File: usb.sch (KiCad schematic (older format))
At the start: 46 parts, among them J6 USB_B_F_X2, J7 USB_B_F_X2, U10 HLF-W2, U4 GL850G, X1 12MHz

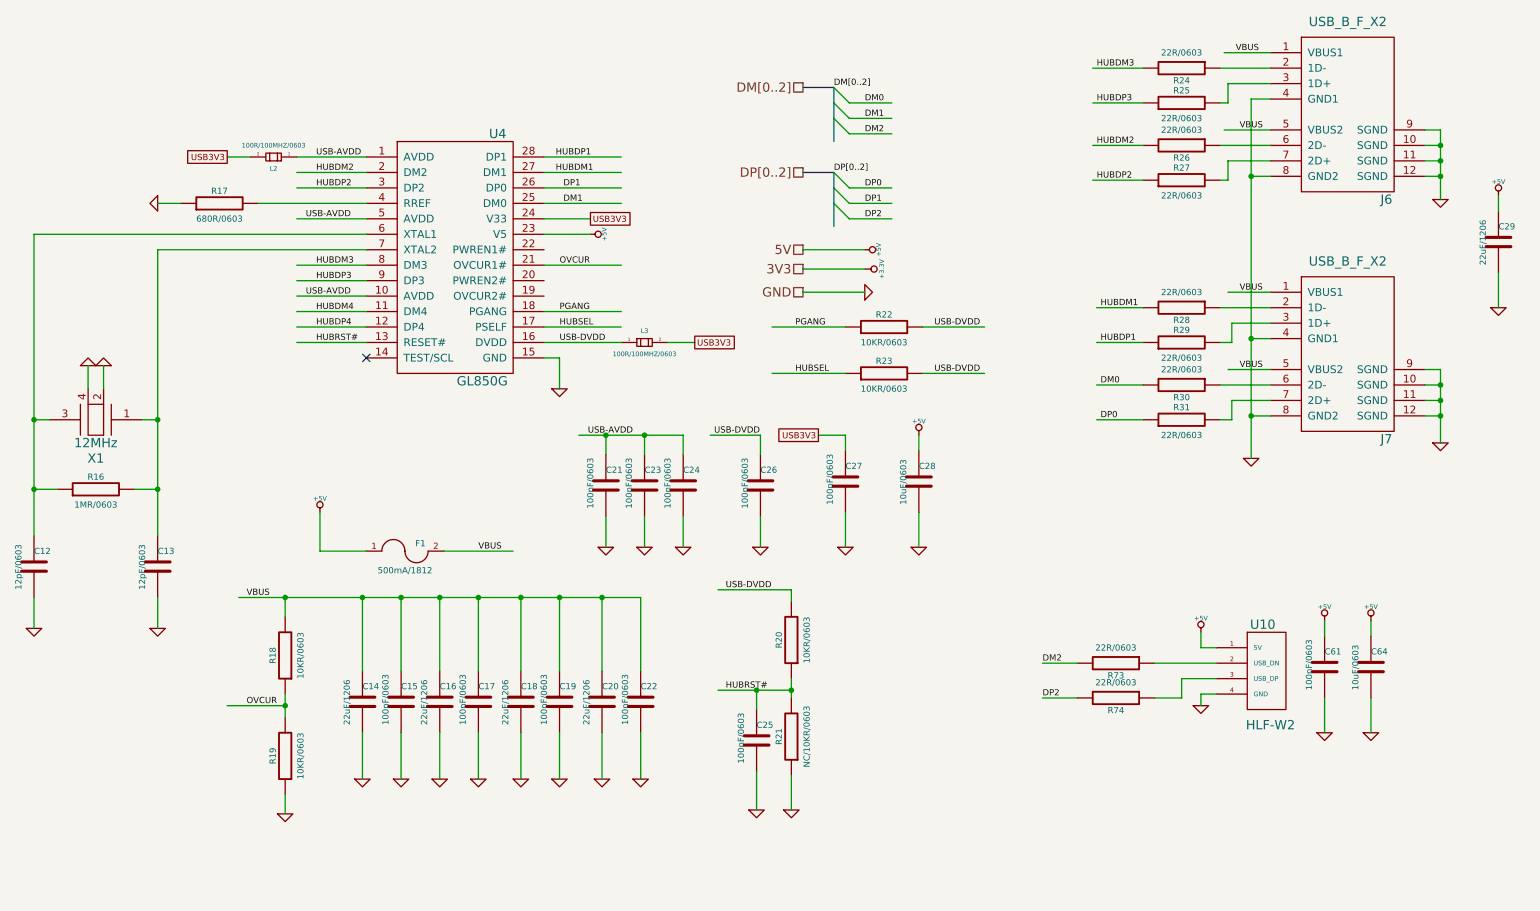
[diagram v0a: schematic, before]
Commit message: 1.4
Fix some issues
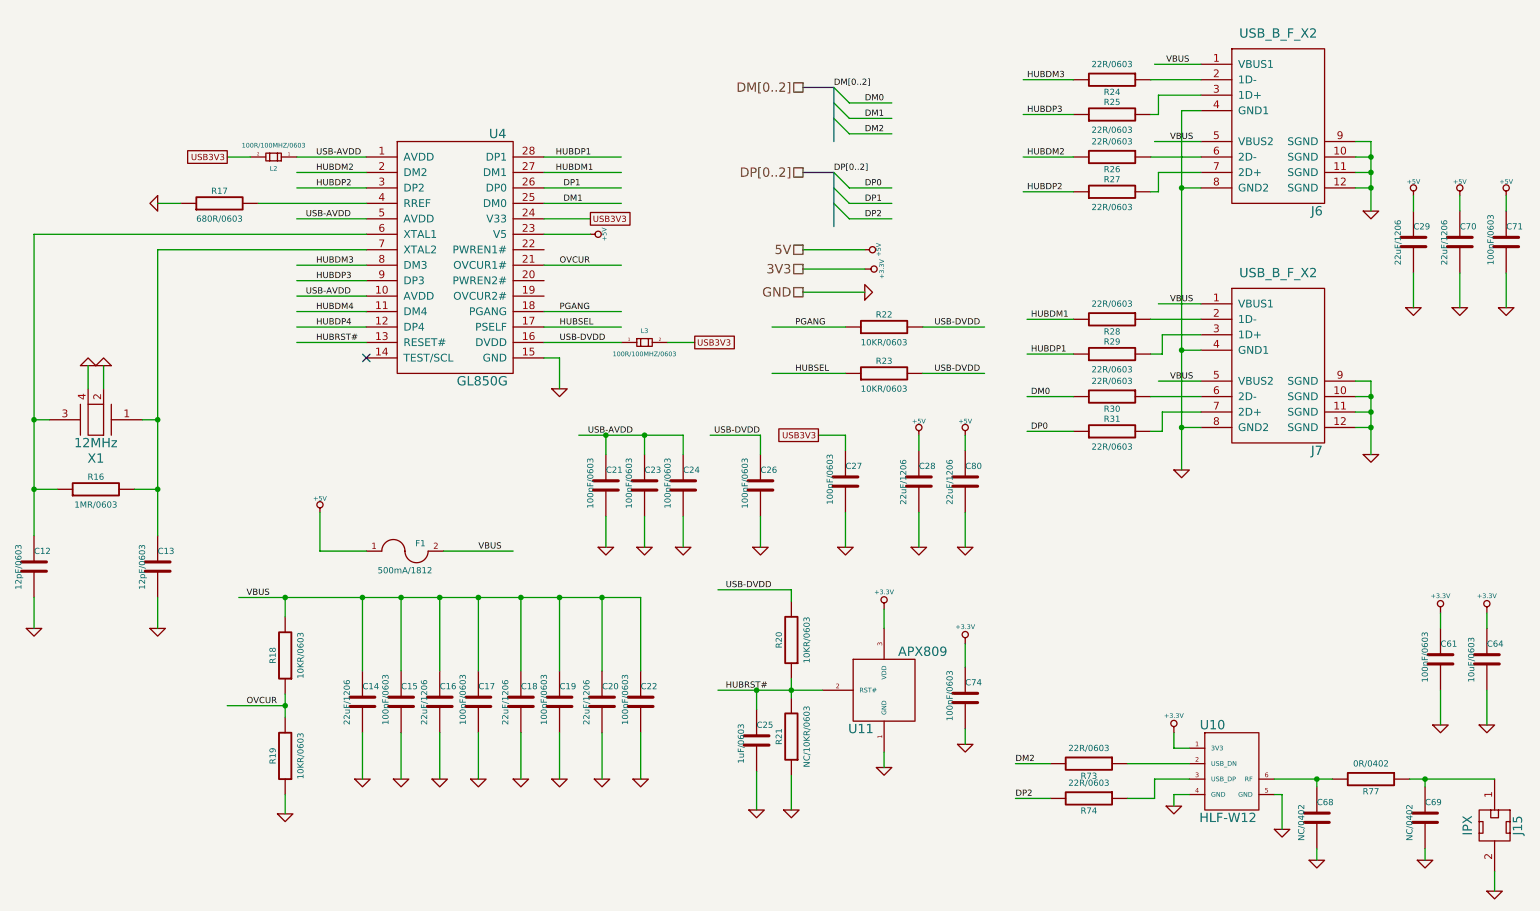
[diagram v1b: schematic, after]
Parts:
- removed U10: HLF-W2, ~, symbol HLF-W2
- added C68, C69: NC/0402, ~, symbol C
- added C70, C80: 22uF/1206, ~, symbol C
- added C71, C74: 100nF/0603, ~, symbol C
- added J15: IPX, ~, symbol IPX
- added R77: 0R/0402, ~, symbol R
- added U10: HLF-W12, ~, symbol HLF-W12
- added U11: APX809, ~, symbol APX809
- C25: value 100nF/0603 -> 1uF/0603
- C28: value 10uF/0603 -> 22uF/1206
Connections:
- wire segments 156 -> 175
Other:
- moved on the sheet: C29, C61, C64, J6, J7, R24, R25, R26, R27, R28, R29, R30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
